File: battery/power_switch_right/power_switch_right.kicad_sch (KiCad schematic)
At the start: 1 part

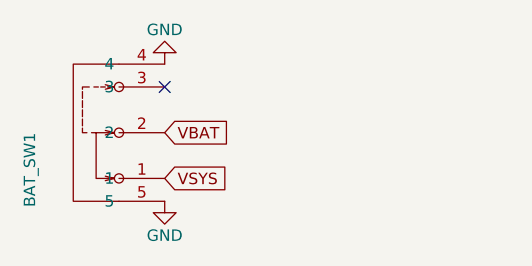
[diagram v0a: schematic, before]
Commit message: use SK12D07VG5
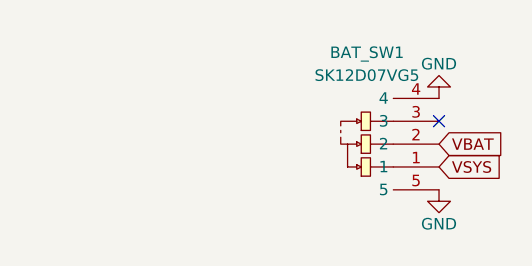
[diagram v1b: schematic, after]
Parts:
- removed BAT_SW1: ~, ErgoCai.pretty:SW-TH_SK12D07VG4, symbol ErgoCai:SK12D07VG4
- added BAT_SW1: SK12D07VG5, ErgoCai.pretty:SW-TH_SK12D07VG5-1, symbol ErgoCai:SK12D07VG5
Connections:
- net GND: now also BAT_SW1.4, BAT_SW1.5
- net VBAT: now also BAT_SW1.2
- net VSYS: now also BAT_SW1.1
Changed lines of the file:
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@@
 	(paper "A4")
 	(no_connect
-		(at 106.68 73.66)
+		(at 137.16 77.47)
 	)
 	(global_label "VBAT"
 		(shape input)
-		(at 106.68 78.74 0)
+		(at 137.16 80.01 0)
 		(fields_autoplaced yes)
 		(effects
@@
 		)
 		(property "Intersheetrefs" "${INTERSHEET_REFS}"
-			(at 114.08 78.74 0)
+			(at 144.56 80.01 0)
 			(effects
 				(font
@@
 	(global_label "VSYS"
 		(shape input)
-		(at 106.68 83.82 0)
+		(at 137.16 82.55 0)
 		(fields_autoplaced yes)
 		(effects
@@
 		)
 		(property "Intersheetrefs" "${INTERSHEET_REFS}"
-			(at 114.2614 83.82 0)
+			(at 144.7414 82.55 0)
 			(effects
 				(font
@@
 	)
 	(symbol
-		(lib_id "ErgoCai:SK12D07VG4")
-		(at 101.6 78.74 90)
+		(lib_id "power:GND")
+		(at 137.16 74.93 180)
 		(unit 1)
 		(exclude_from_sim no)
@@
 		(on_board yes)
 		(dnp no)
-		(property "Reference" "BAT_SW1"
-			(at 91.694 78.74 0)
-			(effects
-				(font
-					(size 1.27 1.27)
-				)
-				(justify right)
-			)
-		)
-		(property "Value" "~"
-			(at 99.0601 85.09 0)
-			(effects
-				(font
-					(size 1.27 1.27)
-				)
-				(justify right)
-			)
-		)
-		(property "Footprint" "ErgoCai.pretty:SW-TH_SK12D07VG4"
-			(at 101.6 78.74 0)
-			(effects
-				(font
-					(size 1.27 1.27)
-				)
-				(justify bottom)
-				(hide yes)
-			)
-		)
-		(property "Datasheet" "https://lcsc.com/product-detail/Toggle-Switches_SHOU-HAN-SK12D07VG4_C393937.html"
-			(at 101.6 78.74 0)
-			(effects
-				(font
-					(size 1.27 1.27)
-				)
-				(hide yes)
-			)
-		)
-		(property "Description" "Switch, dual pole double throw, separate symbols"
-			(at 101.6 78.74 0)
-			(effects
-				(font
-					(size 1.27 1.27)
-				)
-				(hide yes)
-			)
-		)
-		(property "MF" "C&K"
-			(at 101.6 78.74 0)
-			(effects
-				(font
-					(size 1.27 1.27)
-				)
-				(justify bottom)
-				(hide yes)
-			)
-		)
-		(property "Description_1" "Switch Slide ON ON SPDT Side Slide 0.3A 30VDC PC Pins Bracket Mount/Through Hole Bulk"
-			(at 101.6 78.74 0)
-			(effects
-				(font
-					(size 1.27 1.27)
-				)
-				(justify bottom)
-				(hide yes)
-			)
-		)
-		(property "Package" "None"
-			(at 101.6 78.74 0)
-			(effects
-				(font
-					(size 1.27 1.27)
-				)
-				(justify bottom)
-				(hide yes)
-			)
-		)
-		(property "Price" "None"
-			(at 101.6 78.74 0)
-			(effects
-				(font
-					(size 1.27 1.27)
-				)
-				(justify bottom)
-				(hide yes)
-			)
-		)
-		(property "SnapEDA_Link" "https://www.snapeda.com/parts/SK12D07VG4/C%2526K/view-part/?ref=snap"
-			(at 101.6 78.74 0)
-			(effects
-				(font
-					(size 1.27 1.27)
-				)
-				(justify bottom)
-				(hide yes)
-			)
-		)
-		(property "MP" "SK12D07VG4"
-			(at 101.6 78.74 0)
-			(effects
-				(font
-					(size 1.27 1.27)
-				)
-				(justify bottom)
-				(hide yes)
-			)
-		)
-		(property "Availability" "Not in stock"
-			(at 101.6 78.74 0)
-			(effects
-				(font
-					(size 1.27 1.27)
-				)
-				(justify bottom)
-				(hide yes)
-			)
-		)
-		(property "Check_prices" "https://www.snapeda.com/parts/SK12D07VG4/C%2526K/view-part/?ref=eda"
-			(at 101.6 78.74 0)
-			(effects
-				(font
-					(size 1.27 1.27)
-				)
-				(justify bottom)
-				(hide yes)
-			)
-		)
-		(property "LCSC Part" "C393937"
-			(at 119.38 78.74 0)
-			(effects
-				(font
-					(size 1.27 1.27)
-				)
-				(hide yes)
-			)
-		)
-		(pin "5"
-		)
-		(pin "2"
+		(property "Reference" "#PWR02"
+			(at 137.16 68.58 0)
+			(effects
+				(font
+					(size 1.27 1.27)
+				)
+				(hide yes)
+			)
+		)
+		(property "Value" "GND"
+			(at 137.16 71.12 0)
+			(effects
+				(font
+					(size 1.27 1.27)
+				)
+			)
+		)
+		(property "Footprint" ""
+			(at 137.16 74.93 0)
+			(effects
+				(font
+					(size 1.27 1.27)
+				)
+				(hide yes)
+			)
+		)
+		(property "Datasheet" ""
+			(at 137.16 74.93 0)
+			(effects
+				(font
+					(size 1.27 1.27)
+				)
+				(hide yes)
+			)
+		)
+		(property "Description" "Power symbol creates a global label with name \"GND\" , ground"
+			(at 137.16 74.93 0)
+			(effects
+				(font
+					(size 1.27 1.27)
+				)
+				(hide yes)
+			)
 		)
 		(pin "1"
-		)
-		(pin "3"
-		)
-		(pin "4"
 		)
 		(instances
 			(project "power_switch_right"
 				(path "/c041283f-87c4-47d6-8437-14bf29e22537"
-					(reference "BAT_SW1")
+					(reference "#PWR02")
 					(unit 1)
 				)
@@
 	(symbol
 		(lib_id "power:GND")
-		(at 106.68 86.36 0)
+		(at 137.16 85.09 0)
 		(unit 1)
 		(exclude_from_sim no)
@@
 		(dnp no)
 		(property "Reference" "#PWR01"
-			(at 106.68 92.71 0)
+			(at 137.16 91.44 0)
 			(effects
 				(font
@@
 		)
 		(property "Value" "GND"
-			(at 106.68 90.17 0)
+			(at 137.16 88.9 0)
 			(effects
 				(font
@@
 		)
 		(property "Footprint" ""
-			(at 106.68 86.36 0)
+			(at 137.16 85.09 0)
 			(effects
 				(font
@@
 		)
 		(property "Datasheet" ""
-			(at 106.68 86.36 0)
+			(at 137.16 85.09 0)
 			(effects
 				(font
@@
 		)
 		(property "Description" "Power symbol creates a global label with name \"GND\" , ground"
-			(at 106.68 86.36 0)
+			(at 137.16 85.09 0)
 			(effects
 				(font
@@
 	)
 	(symbol
-		(lib_id "power:GND")
-		(at 106.68 71.12 180)
+		(lib_id "ErgoCai:SK12D07VG5")
+		(at 132.08 80.01 90)
 		(unit 1)
 		(exclude_from_sim no)
@@
 		(on_board yes)
 		(dnp no)
-		(property "Reference" "#PWR03"
-			(at 106.68 64.77 0)
-			(effects
-				(font
-					(size 1.27 1.27)
-				)
-				(hide yes)
-			)
-		)
-		(property "Value" "GND"
-			(at 106.68 67.31 0)
-			(effects
-				(font
-					(size 1.27 1.27)
-				)
-			)
-		)
-		(property "Footprint" ""
-			(at 106.68 71.12 0)
-			(effects
-				(font
-					(size 1.27 1.27)
-				)
-				(hide yes)
-			)
-		)
-		(property "Datasheet" ""
-			(at 106.68 71.12 0)
-			(effects
-				(font
-					(size 1.27 1.27)
-				)
-				(hide yes)
-			)
-		)
-		(property "Description" "Power symbol creates a global label with name \"GND\" , ground"
-			(at 106.68 71.12 0)
-			(effects
-				(font
-					(size 1.27 1.27)
-				)
-				(hide yes)
-			)
+		(fields_autoplaced yes)
+		(property "Reference" "BAT_SW1"
+			(at 129.16 69.85 90)
+			(effects
+				(font
+					(size 1.27 1.27)
+				)
+			)
+		)
+		(property "Value" "SK12D07VG5"
+			(at 129.16 72.39 90)
+			(effects
+				(font
+					(size 1.27 1.27)
+				)
+			)
+		)
+		(property "Footprint" "ErgoCai.pretty:SW-TH_SK12D07VG5-1"
+			(at 144.78 80.01 0)
+			(effects
+				(font
+					(size 1.27 1.27)
+				)
+				(hide yes)
+			)
+		)
+		(property "Datasheet" "https://lcsc.com/product-detail/Toggle-Switches_SHOU-HAN-SK12D07VG5_C431548.html"
+			(at 147.32 80.01 0)
+			(effects
+				(font
+					(size 1.27 1.27)
+				)
+				(hide yes)
+			)
+		)
+		(property "Description" ""
+			(at 132.08 80.01 0)
+			(effects
+				(font
+					(size 1.27 1.27)
+				)
+				(hide yes)
+			)
+		)
+		(property "LCSC Part" "C431548"
+			(at 149.86 80.01 0)
+			(effects
+				(font
+					(size 1.27 1.27)
+				)
+				(hide yes)
+			)
+		)
+		(pin "5"
 		)
 		(pin "1"
 		)
+		(pin "2"
+		)
+		(pin "3"
+		)
+		(pin "4"
+		)
 		(instances
-			(project "power_switch_right"
+			(project ""
 				(path "/c041283f-87c4-47d6-8437-14bf29e22537"
-					(reference "#PWR03")
+					(reference "BAT_SW1")
 					(unit 1)
 				)

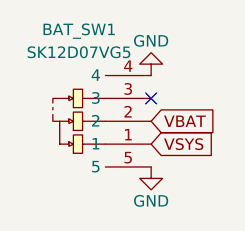
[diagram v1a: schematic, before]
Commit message: update power switch
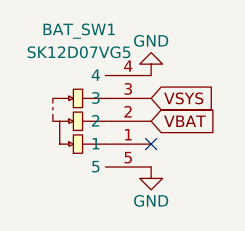
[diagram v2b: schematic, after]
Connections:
- net VSYS: now also BAT_SW1.3; no longer BAT_SW1.1
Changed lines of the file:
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@@
 	(paper "A4")
 	(no_connect
-		(at 137.16 77.47)
+		(at 137.16 82.55)
 	)
 	(global_label "VBAT"
@@
 	(global_label "VSYS"
 		(shape input)
-		(at 137.16 82.55 0)
+		(at 137.16 77.47 0)
 		(fields_autoplaced yes)
 		(effects
@@
 		)
 		(property "Intersheetrefs" "${INTERSHEET_REFS}"
-			(at 144.7414 82.55 0)
+			(at 144.7414 77.47 0)
 			(effects
 				(font
@@
 		)
 		(instances
-			(project ""
+			(project "power_switch_right"
 				(path "/c041283f-87c4-47d6-8437-14bf29e22537"
 					(reference "BAT_SW1")
